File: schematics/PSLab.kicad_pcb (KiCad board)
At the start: 4 copper layers, 99 x 53.3 mm, 193 parts, among them J1 DoublePins, J11 Li-Ion Battery, J2 Power Pins, J3 Wave Generator, J4 I2C, J5 I2C, J6 ESP01, J7 UART, J8 Battery Switch, J9 SPI, P1 SDCard, P2 USB_C - Generic, Q1 MMBT3906, Q2 MMBT3904, Q3 MMBT3906, SW1 SW_MEC_5E, SW2 SW_MEC_5E, SW3 SW_MEC_5E, U1 FP6291, U10 TL082, U11 TL082, U12 74HC4051, U13 MAX5400, U14 MAX5400, U15 CP2102N-xxx-xQFN20x, U16 SP0503BAHT, U17 IP5189T, U18 TL082, U19 MCP4822, U2 74HC126, U20 MCP4822, U3 PIC24EP256GP204, U4 DS1307Z+, U5 TP7660H, U6 HT7333-A, U7 LM324, U8 TL082, U9 TL082, X2 32.768 kHz, Y1 12 MHz

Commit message: chore: update PCB
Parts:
- added R72: 10k, Resistor_SMD:R_0603_1608Metric, F.Cu at (166.6, 88.0)
- added R73: 10k, Resistor_SMD:R_0603_1608Metric, F.Cu at (169.9, 88.0)
- moved C40 4.71 mm to (151.7, 85.7), turned to 0 degrees
- moved R52 3.52 mm to (173.3, 88.0)
- moved C1 2.81 mm to (162.6, 87.9)
- moved SW1 2.29 mm to (144.9, 84.0)
- moved SW2 2.23 mm to (144.9, 64.2)
- moved D3 1.78 mm to (173.1, 89.9)
- moved C3 1.70 mm to (147.7, 64.2)
- moved C33 1.69 mm to (151.7, 87.3)
- moved C9 1.60 mm to (159.6, 87.9)
- moved R2 1.23 mm to (149.3, 64.2)
- moved C15 1.21 mm to (129.3, 78.9)
- moved SW3 1.20 mm to (139.7, 64.2)
- moved X2 0.96 mm to (172.6, 93.5)
- moved R15 0.71 mm to (150.9, 89.7)
- moved R3 0.70 mm to (150.9, 64.2)
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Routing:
- net GND: track 220.8 -> 204.8 mm, vias 163 -> 167
- net VDDA: track 127.8 -> 138.5 mm
- net SD.CS: track 68.0 -> 72.8 mm, vias 4 -> 5
- net SPI.CS: track 93.1 -> 96.2 mm, vias 5 -> 6
- net +5V: track 169.5 -> 166.6 mm
- net SQR4_: track 35.3 -> 38.0 mm
- net Net-(C33-Pad2): track 8.35 -> 5.71 mm
- net STAT: track 15.5 -> 17.6 mm
- net MCLR: track 39.4 -> 37.5 mm
- net SDA: track 72.0 -> 70.1 mm
- net +3V3: track 159.8 -> 158.2 mm, vias 5 -> 6
- net Net-(BT1-Pad1): track 34.6 -> 33.0 mm
- net Net-(C40-Pad1): track 9.64 -> 8.13 mm
- net BOOT: track 33.3 -> 32.1 mm, vias 4 -> 2
- net Net-(D3-Pad2): track 1.71 -> 2.75 mm
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
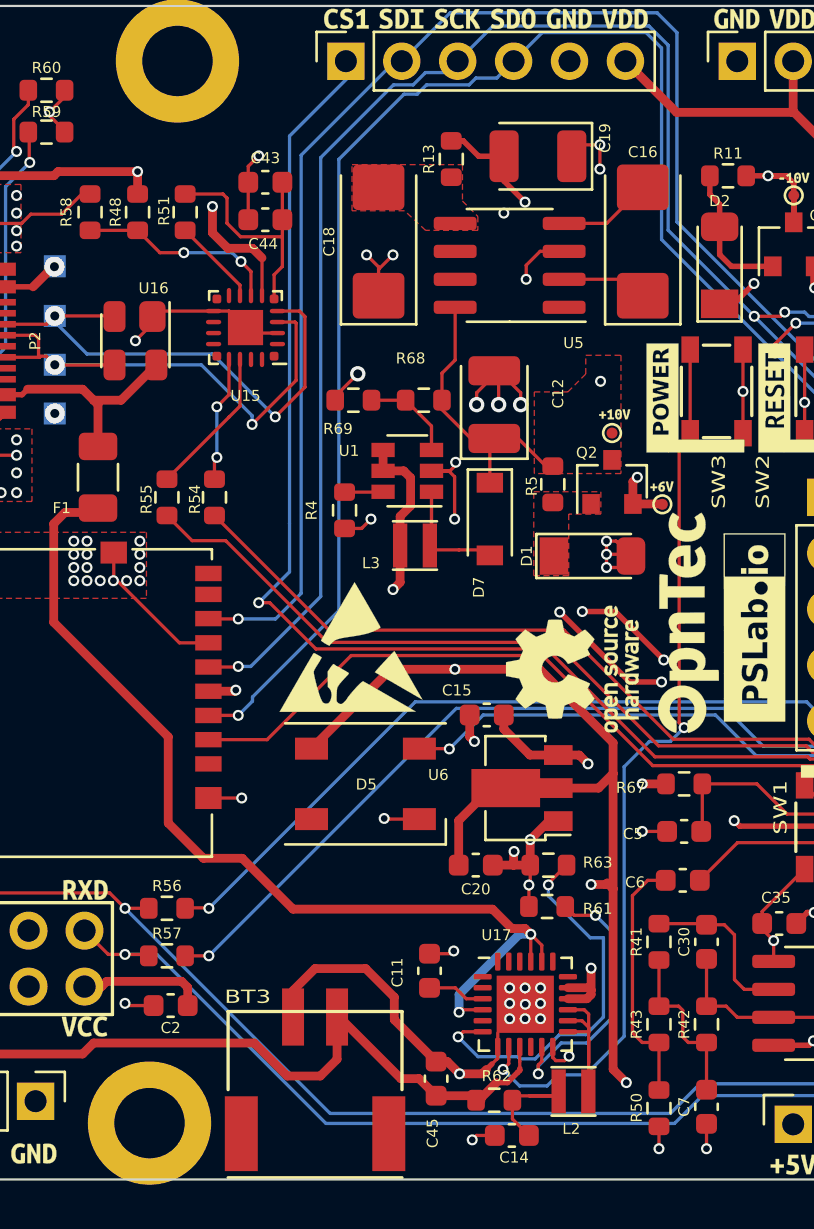
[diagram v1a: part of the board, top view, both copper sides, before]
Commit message: chore: Delete 100uF capacitors
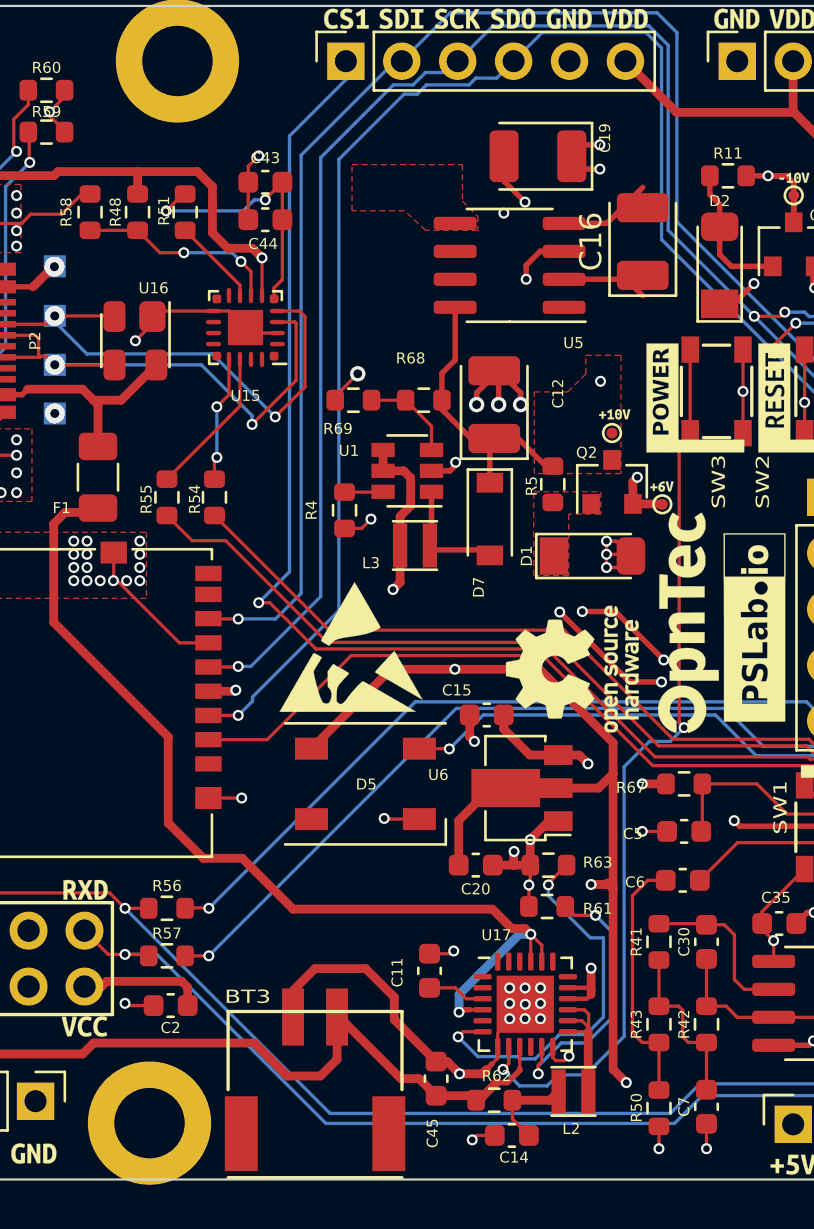
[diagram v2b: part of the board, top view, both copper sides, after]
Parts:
- removed C18: 100uF, Capacitor_Tantalum_SMD:CP_EIA-6032-28_Kemet-C
- removed R13: 18, Resistor_SMD:R_0603_1608Metric
- C12: value 100uF -> 33uF
- C16: value 100uF -> 33uF; footprint Capacitor_Tantalum_SMD:CP_EIA-6032-28_Kemet-C -> Capacitor_Tantalum_SMD:CP_EIA-3528-21_Kemet-B
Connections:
- U5 pad 5: Net-(C18-Pad2) -> -10V
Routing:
- net +5V: track 166.6 -> 159.4 mm, vias 8 -> 7
- net GND: track 204.8 -> 199.2 mm, vias 167 -> 164
- net -10V: track 106.8 -> 104.1 mm
- net Net-(L2-Pad1): track 7.79 -> 6.60 mm
- net /CP2102_Vreg: track 11.4 -> 12.5 mm, vias 0 -> 2
- net Net-(C14-Pad1): track 5.19 -> 4.18 mm
- added copper zone on F.Cu, net -10V
- removed copper zone on F.Cu, net Net-(C18-Pad2)

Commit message: Temp9
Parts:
- removed J11: Li-Ion Battery, Connector_PinHeader_2.54mm:PinHeader_1x02_P2.54mm_Vertical
- removed J8: Battery Switch, Connector_PinHeader_2.54mm:PinHeader_1x02_P2.54mm_Vertical
- added C18: 100nF, Capacitor_SMD:C_0603_1608Metric, F.Cu at (130.5, 65.3)
- added C46: 10uF, Capacitor_SMD:C_0603_1608Metric, F.Cu at (132.1, 65.3)
- C12: value 33uF -> 10uF; footprint Capacitor_Tantalum_SMD:CP_EIA-3528-21_Kemet-B -> Capacitor_SMD:C_0603_1608Metric
- moved C16 4.07 mm to (132.7, 59.2)
- moved C19 3.52 mm to (128.2, 54.4)
- moved U5 3.52 mm to (126.9, 59.4)
- moved C12 0.86 mm to (128.9, 65.3)
- moved C11 0.74 mm to (127.4, 90.5)
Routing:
- net /BAT+: track 35.3 -> 11.7 mm
- net Net-(J11-Pad2): track 4.53 -> 0.00 mm
- net -10V: track 104.1 -> 107.8 mm, vias 10 -> 9
- net +3V3: track 158.2 -> 155.6 mm
- net +10V: track 94.5 -> 96.6 mm
- net GND: track 199.2 -> 198.1 mm, vias 164 -> 163
- net VDDA: track 138.5 -> 137.6 mm
- net Net-(C16-Pad2): track 4.24 -> 3.40 mm
- net CS3: track 43.9 -> 43.1 mm
- net Net-(C11-Pad1): track 2.62 -> 1.89 mm
- removed copper zone on F.Cu, net -10V
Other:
- board text added: "- +"

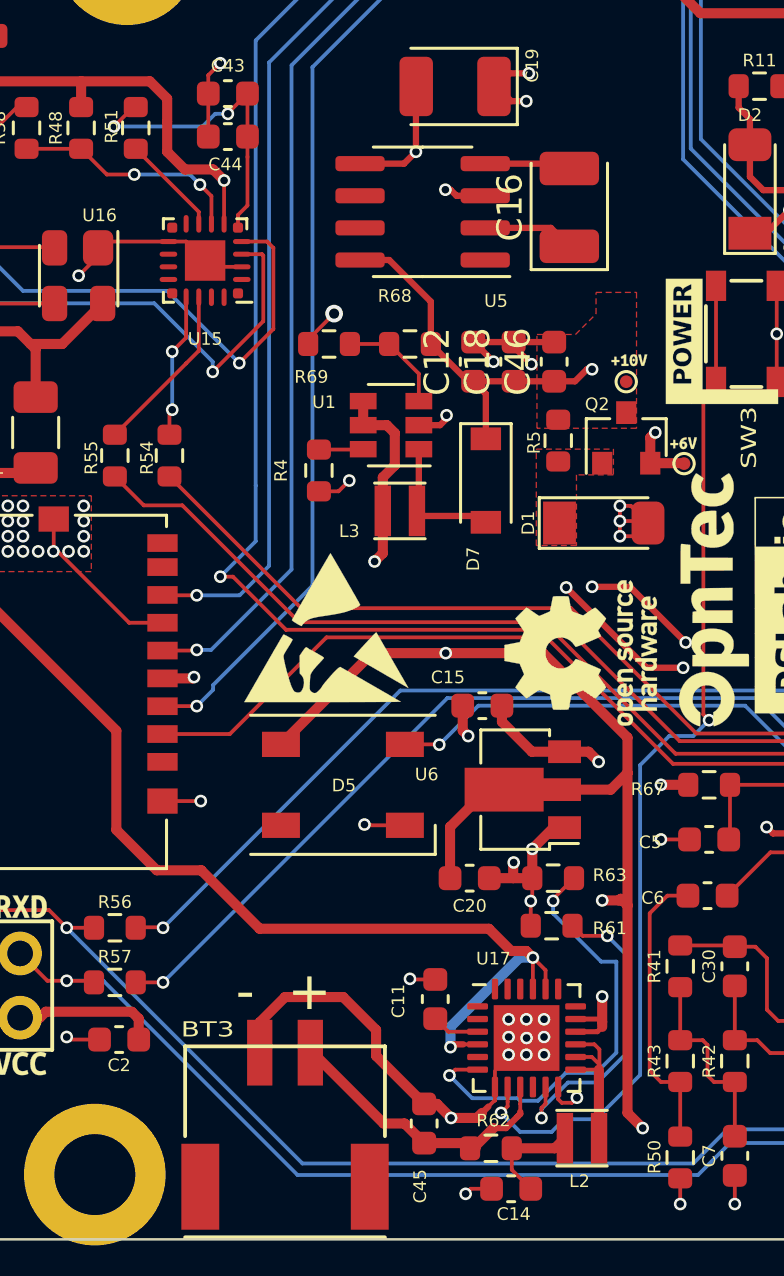
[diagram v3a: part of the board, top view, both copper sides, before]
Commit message: refactor: replace IP5189T to IP5219T
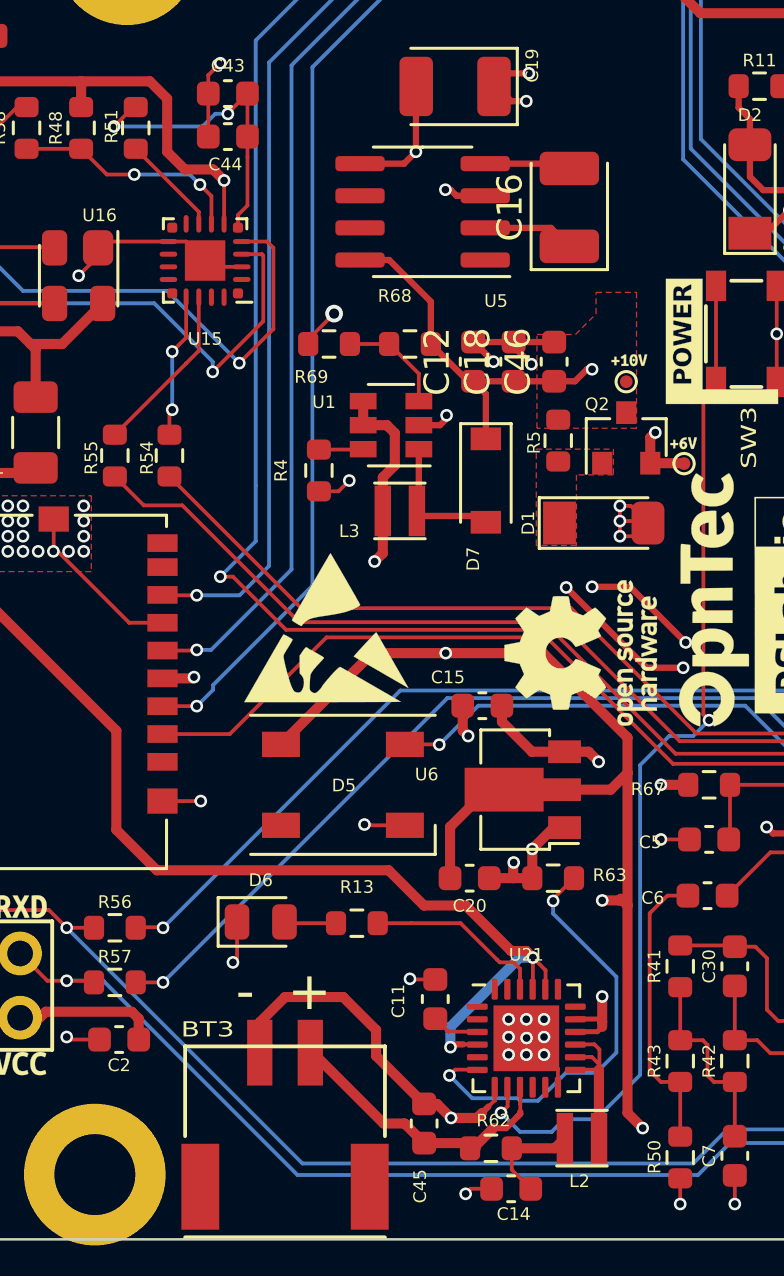
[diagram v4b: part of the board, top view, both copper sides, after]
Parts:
- removed R61: 200k, Resistor_SMD:R_0603_1608Metric
- removed U17: IP5189T, Package_DFN_QFN:QFN-24-1EP_4x4mm_P0.5mm_EP2.6x2.6mm
- added D6: GREEN, LED_SMD:LED_0805_2012Metric, F.Cu at (120.5, 87.5)
- added R13: 5.1k, Resistor_SMD:R_0603_1608Metric, F.Cu at (124.3, 87.5)
- added U21: IP5219, Package_DFN_QFN:QFN-24-1EP_4x4mm_P0.5mm_EP2.6x2.6mm, F.Cu at (131.0, 92.0)
- R63: value 51k -> 0
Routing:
- net Net-(R61-Pad1): track 12.5 -> 0.00 mm, vias 2 -> 0
- net Net-(R13-Pad2): track 0.00 -> 7.18 mm
- net Net-(D6-Pad2): track 0.00 -> 2.06 mm
- net GND: track 198.1 -> 197.4 mm, vias 163 -> 162

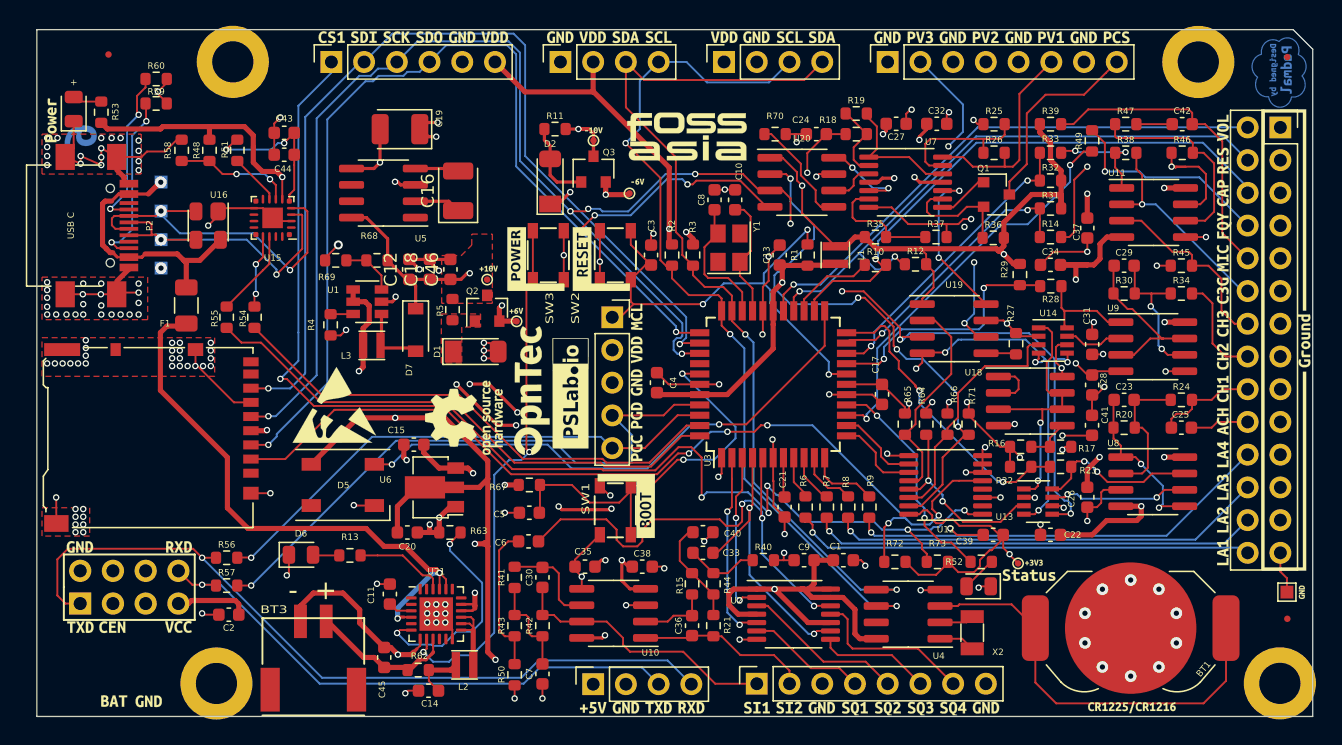
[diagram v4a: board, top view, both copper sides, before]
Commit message: chore: update tf card footprint
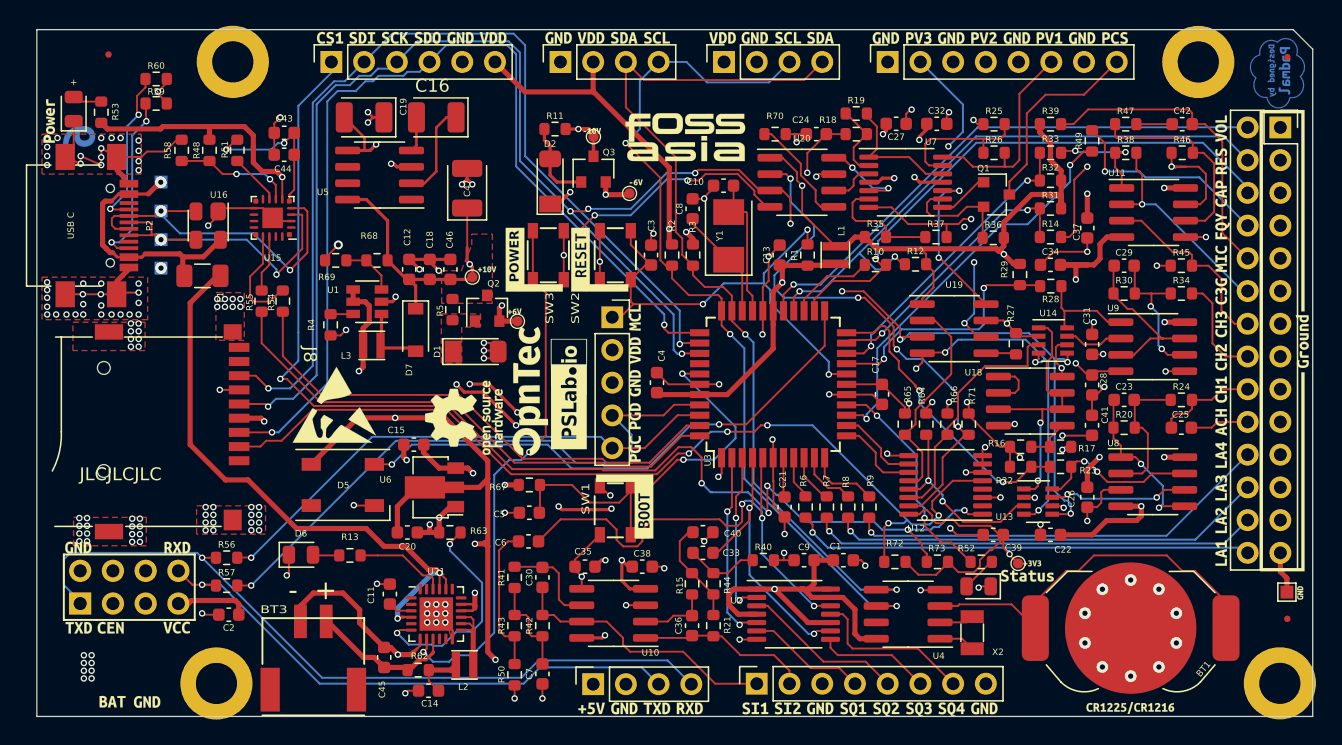
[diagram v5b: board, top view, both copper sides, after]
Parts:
- removed P1: SDCard, PSLab:microSD_HC_Hirose_DM3AT-SF-PEJM5
- added C47: 33uF, Capacitor_Tantalum_SMD:CP_EIA-3528-21_Kemet-B, F.Cu at (133.4, 59.0)
- added J8: Micro_SD_Card_Det_9_pin, PSLab:TF-015, F.Cu at (115.7, 77.9)
- C1, C13, C17, C2, C22, C24, C25, C26, C27, C28, C3, C31, C32, C34, C35, C37, C38, C39, C4, C41, C43, C5, C9: value 0.1uF -> 100nF
- L1: value 10uH -> 4.7uH
- L2, L3: value 4.7uH -> 3.3uH
- R1, R10, R14, R16, R17, R18, R19, R21, R25, R31, R32, R33, R35, R37, R38, R39, R42, R58, R67: value 10K -> 10k
- R12, R15, R2, R26, R3, R41, R43, R44, R48, R52, R53, R59, R60: value 5K1 -> 5.1k
- TP1, TP2, TP3, TP5, TP6: footprint PSLab:Voltage_Test_Point -> PSLab:Test_Point_0.8mm
- Y1: value 12 MHz -> 12MHz; footprint Crystal:Crystal_SMD_3225-4Pin_3.2x2.5mm -> Crystal:Crystal_SMD_5032-2Pin_5.0x3.2mm
- moved C16 5.95 mm to (131.0, 53.5), turned to 180 degrees
- moved R55 2.99 mm to (117.5, 67.8)
- moved C19 2.93 mm to (125.4, 53.5)
- moved F1 2.62 mm to (112.8, 65.8), turned to 0 degrees
- moved R54 2.53 mm to (119.1, 67.8)
- moved C8 1.84 mm to (150.9, 60.6)
- moved U5 1.43 mm to (126.6, 58.0)
- moved C10 1.42 mm to (153.3, 58.8), turned to 180 degrees
- moved TP6 1.17 mm to (133.8, 65.9)
- moved Y1 0.91 mm to (153.7, 62.7)
- moved TP5 0.30 mm to (143.2, 55.0)
- moved Z9 0.14 mm to (149.2, 50.0)
- moved TP2 0.06 mm to (137.3, 69.3)
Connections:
- Y1 pad 1: /OSC_IN -> /OSC_OUT
- Y1 pad 2: (no net) -> /OSC_IN
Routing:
- net GND: track 197.4 -> 190.0 mm, vias 162 -> 187
- net +10V: track 96.6 -> 103.9 mm
- net Net-(BT1-Pad1): track 33.0 -> 27.6 mm
- net Net-(C16-Pad1): track 3.63 -> 7.57 mm
- net SDO: track 139.0 -> 142.3 mm
- net +3V3: track 155.6 -> 158.2 mm
- net Net-(R54-Pad1): track 5.71 -> 8.19 mm, vias 2 -> 0
- net Net-(R55-Pad1): track 6.81 -> 4.44 mm
- net /OSC_OUT: track 10.9 -> 8.74 mm
- net RxD2: track 60.9 -> 59.3 mm
- net SDI: track 74.9 -> 76.1 mm
- net /VINPUT: track 45.5 -> 46.7 mm
- net SPI.CS: track 96.2 -> 95.2 mm
- net /VUSBIN: track 21.1 -> 20.2 mm
- net /TxD: track 42.2 -> 41.4 mm
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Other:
- board text added: "JLCJLCJLC"
